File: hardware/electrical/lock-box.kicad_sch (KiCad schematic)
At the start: 0 parts

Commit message: feat(eda): add indicator schematics
leds and buzzers
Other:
- added sheet indicators (indicators.kicad_sch)
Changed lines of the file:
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@@
 	(generator_version "9.0")
 	(paper "A4")
+	(sheet
+		(at 225.425 76.2)
+		(size 22.86 43.18)
+		(exclude_from_sim no)
+		(in_bom yes)
+		(on_board yes)
+		(dnp no)
+		(fields_autoplaced yes)
+		(stroke
+			(width 0.1524)
+			(type solid)
+		)
+		(fill
+			(color 0 0 0 0.0000)
+		)
+		(property "Sheetname" "indicators"
+			(at 225.425 75.4884 0)
+			(effects
+				(font
+					(size 1.27 1.27)
+				)
+				(justify left bottom)
+			)
+		)
+		(property "Sheetfile" "indicators.kicad_sch"
+			(at 225.425 119.9646 0)
+			(effects
+				(font
+					(size 1.27 1.27)
+				)
+				(justify left top)
+			)
+		)
+		(pin "3rd Digit" input
+			(at 225.425 86.995 180)
+			(effects
+				(font
+					(size 1.27 1.27)
+				)
+				(justify left)
+			)
+		)
+		(pin "2nd Digit" input
+			(at 225.425 83.185 180)
+			(effects
+				(font
+					(size 1.27 1.27)
+				)
+				(justify left)
+			)
+		)
+		(pin "Error LED" input
+			(at 225.425 100.965 180)
+			(effects
+				(font
+					(size 1.27 1.27)
+				)
+				(justify left)
+			)
+		)
+		(pin "1st Digit" input
+			(at 225.425 79.375 180)
+			(effects
+				(font
+					(size 1.27 1.27)
+				)
+				(justify left)
+			)
+		)
+		(pin "4th Digit" input
+			(at 225.425 90.805 180)
+			(effects
+				(font
+					(size 1.27 1.27)
+				)
+				(justify left)
+			)
+		)
+		(pin "Buzzer" input
+			(at 225.425 109.855 180)
+			(effects
+				(font
+					(size 1.27 1.27)
+				)
+				(justify left)
+			)
+		)
+		(instances
+			(project "lock-box"
+				(path "/42416d92-fe63-4085-b8a4-c2081c458f3d"
+					(page "2")
+				)
+			)
+		)
+	)
 	(sheet_instances
 		(path "/"

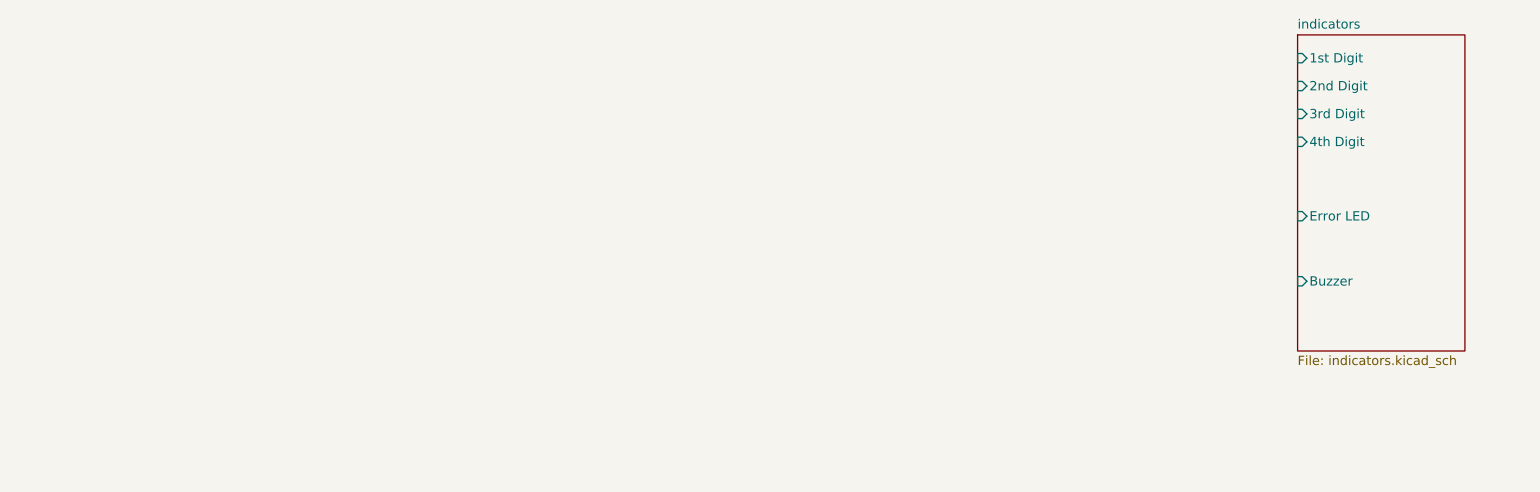
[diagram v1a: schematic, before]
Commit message: (eda): add power subcircuit
add a LDO linear voltage regulator for 3.3V
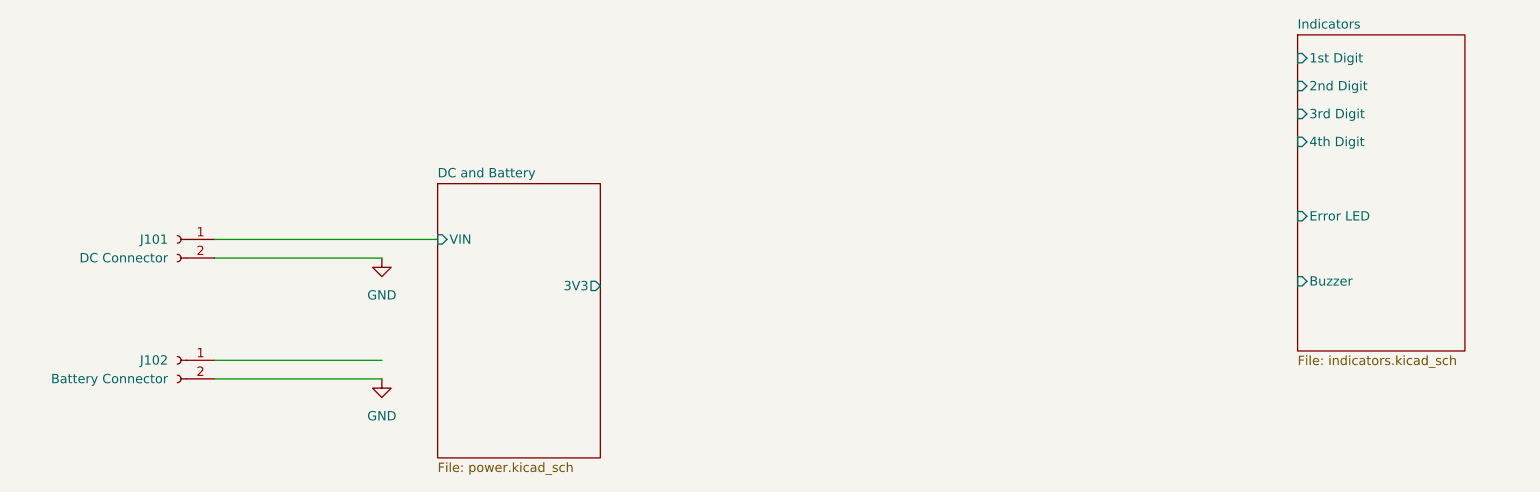
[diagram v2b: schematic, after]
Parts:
- added J101: DC Connector, Connector_JST:JST_PH_S2B-PH-K_1x02_P2.00mm_Horizontal, symbol Connector:Conn_01x02_Socket
- added J102: Battery Connector, Connector_JST:JST_PH_S2B-PH-K_1x02_P2.00mm_Horizontal, symbol Connector:Conn_01x02_Socket
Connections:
- new net DC and Battery/VIN: J101.1 (Pin_1)
- new net GND: J101.2 (Pin_2), J102.2 (Pin_2)
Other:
- sheet indicators renamed Indicators
- added sheet DC and Battery (power.kicad_sch)
